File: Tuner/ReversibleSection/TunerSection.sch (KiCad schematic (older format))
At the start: 68 parts, among them J1 Conn_01x03, J10 Conn_01x02, J11 Conn_01x05, J12 Conn_01x01, J13 Conn_01x01, J14 Conn_01x01, J15 Conn_01x01, J2 Conn_01x03, J3 Conn_01x03, J4 Conn_01x03, J5 Conn_01x03, J6 Conn_01x03, J7 Conn_01x03, J8 Conn_01x02, J9 Conn_01x02, U1 MCP23008, U2 ULN2803A

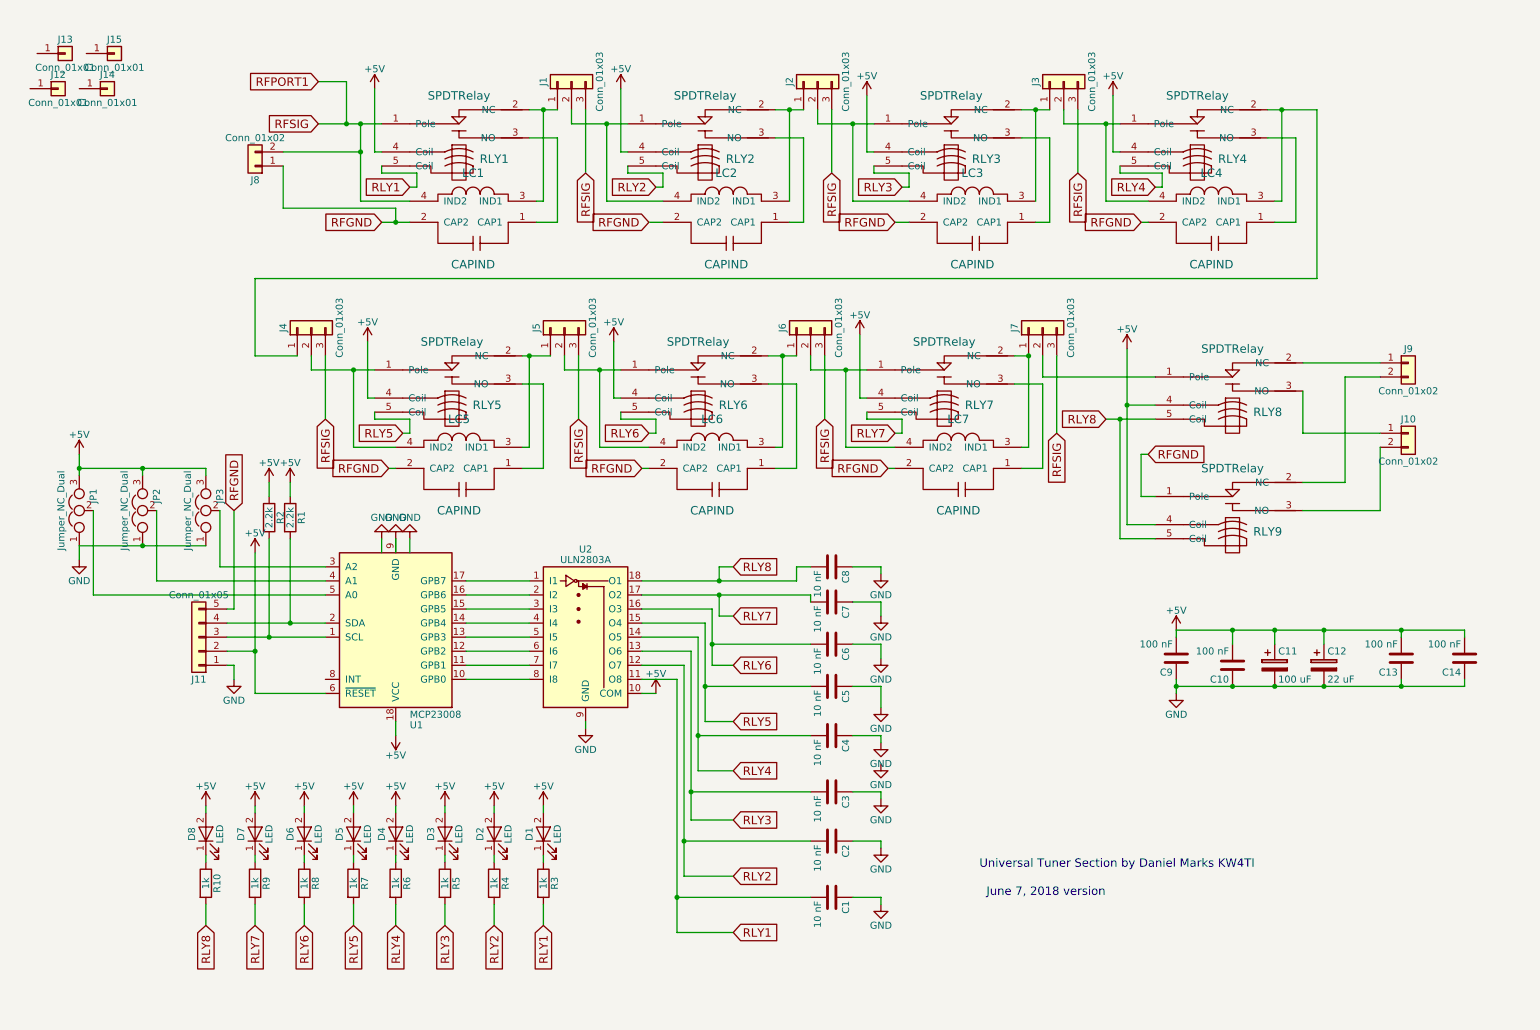
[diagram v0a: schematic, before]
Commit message: Added RF Shielding to ReversibleSection
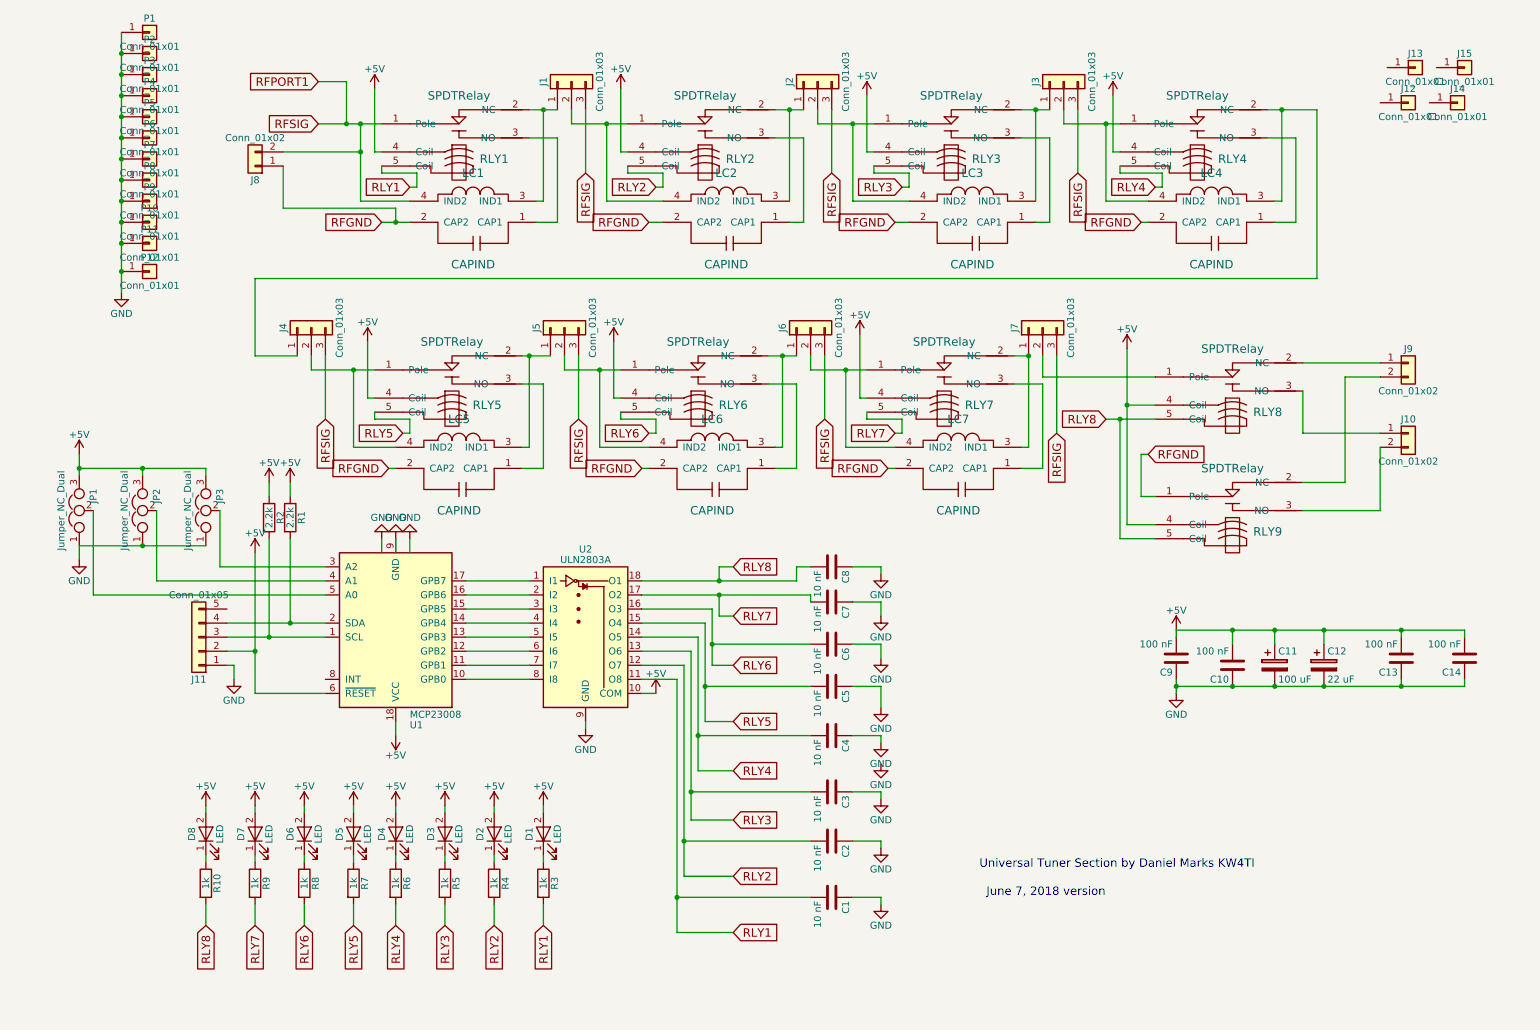
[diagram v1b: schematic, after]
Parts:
- added P1, P10, P11, P12, P2, P3, P4, P5, P6, P7, P8, P9: Conn_01x01, Pin_Headers:Pin_Header_Straight_1x01_Pitch2.54mm, symbol Conn_01x01
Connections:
- net GND: now also P1.1 (Pin_1), P10.1 (Pin_1), P11.1 (Pin_1), P12.1 (Pin_1), P2.1 (Pin_1), P3.1 (Pin_1), P4.1 (Pin_1), P5.1 (Pin_1), P6.1 (Pin_1), P7.1 (Pin_1), P8.1 (Pin_1), P9.1 (Pin_1)
- net RFGND: no longer J11.5 (Pin_5)
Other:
- moved on the sheet: J12, J13, J14, J15

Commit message: Modified RelayControl and Reversible Section to Isolate Digital from Analog sections using RF chokes
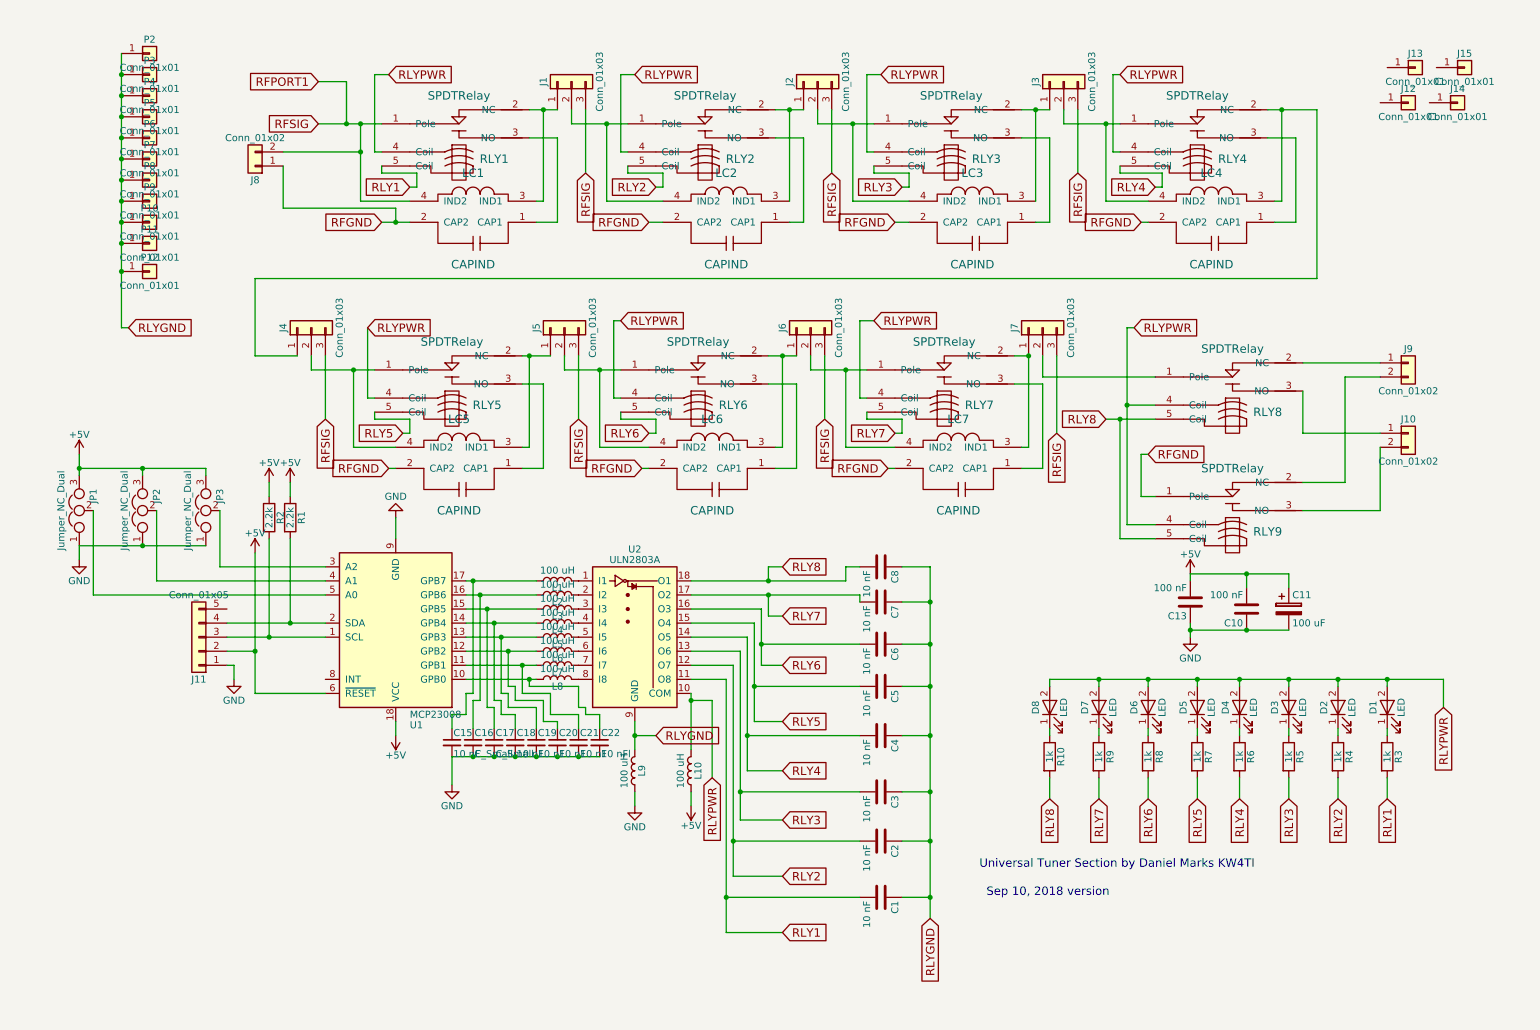
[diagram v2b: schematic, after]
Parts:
- removed C12: 22 uF, Capacitors_THT:CP_Radial_D5.0mm_P2.50mm, symbol CP
- removed C14, C9: 100 nF, Capacitors_THT:C_Disc_D5.0mm_W2.5mm_P2.50mm, symbol C
- removed P1: Conn_01x01, Pin_Headers:Pin_Header_Straight_1x01_Pitch2.54mm, symbol Conn_01x01
- added C15, C18, C19, C20, C21: 10 nF, Capacitors_THT:C_Disc_D5.0mm_W2.5mm_P2.50mm, symbol C_Small
- added C16, C17: C_Small, Capacitors_THT:C_Disc_D5.0mm_W2.5mm_P2.50mm, symbol C_Small
- added C22: 10 nFl, Capacitors_THT:C_Disc_D5.0mm_W2.5mm_P2.50mm, symbol C_Small
- added L1, L10, L2, L3, L4, L5, L6, L7, L8, L9: 100 uH, Inductors_THT:L_Axial_L5.3mm_D2.2mm_P7.62mm_Horizontal_Vishay_IM-1, symbol L
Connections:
- net +5V: now also L10.1; no longer D1.2 (A), D2.2 (A), D3.2 (A), D4.2 (A), D5.2 (A), D6.2 (A), D7.2 (A), D8.2 (A), RLY1.4 (Coil), RLY2.4 (Coil), RLY3.4 (Coil), RLY4.4 (Coil), RLY5.4 (Coil), RLY6.4 (Coil), RLY7.4 (Coil), RLY8.4 (Coil), RLY9.4 (Coil), U2.10 (COM)
- net GND: now also C15.2, C16.2, C17.2, C18.2, C19.2, C20.2, C21.2, C22.2, L9.1; no longer C1.1, C2.1, C3.1, C4.1, C5.1, C6.1, C7.1, C8.1, P10.1 (Pin_1), P11.1 (Pin_1), P12.1 (Pin_1), P2.1 (Pin_1), P3.1 (Pin_1), P4.1 (Pin_1), P5.1 (Pin_1), P6.1 (Pin_1), P7.1 (Pin_1), P8.1 (Pin_1), P9.1 (Pin_1), U2.9 (GND)
- net at U2.1 (I1): now also L1.2; no longer U1.17 (GPB7)
- net at U2.2 (I2): now also L2.2; no longer U1.16 (GPB6)
- net at U2.3 (I3): now also L3.2; no longer U1.15 (GPB5)
- net at U2.4 (I4): now also L4.2; no longer U1.14 (GPB4)
- net at U2.5 (I5): now also L5.2; no longer U1.13 (GPB3)
- net at U2.6 (I6): now also L6.2; no longer U1.12 (GPB2)
- net at U2.7 (I7): now also L7.2; no longer U1.11 (GPB1)
- net at U2.8 (I8): now also L8.2; no longer U1.10 (GPB0)
- new net: C22.1, L8.1, U1.10 (GPB0)
- new net: C21.1, L7.1, U1.11 (GPB1)
- new net: C20.1, L6.1, U1.12 (GPB2)
- new net: C19.1, L5.1, U1.13 (GPB3)
- new net: C18.1, L4.1, U1.14 (GPB4)
- new net: C17.1, L3.1, U1.15 (GPB5)
- new net: C16.1, L2.1, U1.16 (GPB6)
- new net: C15.1, L1.1, U1.17 (GPB7)
- new net RLYGND: C1.1, C2.1, C3.1, C4.1, C5.1, C6.1, C7.1, C8.1, L9.2, P10.1 (Pin_1), P11.1 (Pin_1), P12.1 (Pin_1), P2.1 (Pin_1), P3.1 (Pin_1), P4.1 (Pin_1), P5.1 (Pin_1), P6.1 (Pin_1), P7.1 (Pin_1), P8.1 (Pin_1), P9.1 (Pin_1), U2.9 (GND)
- new net RLYPWR: D1.2 (A), D2.2 (A), D3.2 (A), D4.2 (A), D5.2 (A), D6.2 (A), D7.2 (A), D8.2 (A), L10.2, RLY1.4 (Coil), RLY2.4 (Coil), RLY3.4 (Coil), RLY4.4 (Coil), RLY5.4 (Coil), RLY6.4 (Coil), RLY7.4 (Coil), RLY8.4 (Coil), RLY9.4 (Coil), U2.10 (COM)
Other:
- note added: "Sep 10, 2018 version"
- note removed: "June 7, 2018 version"
- moved on the sheet: C1, C10, C11, C13, C2, C3, C4, C5, C6, C7, C8, D1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

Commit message: Added extra filtering and shunt to RF ground
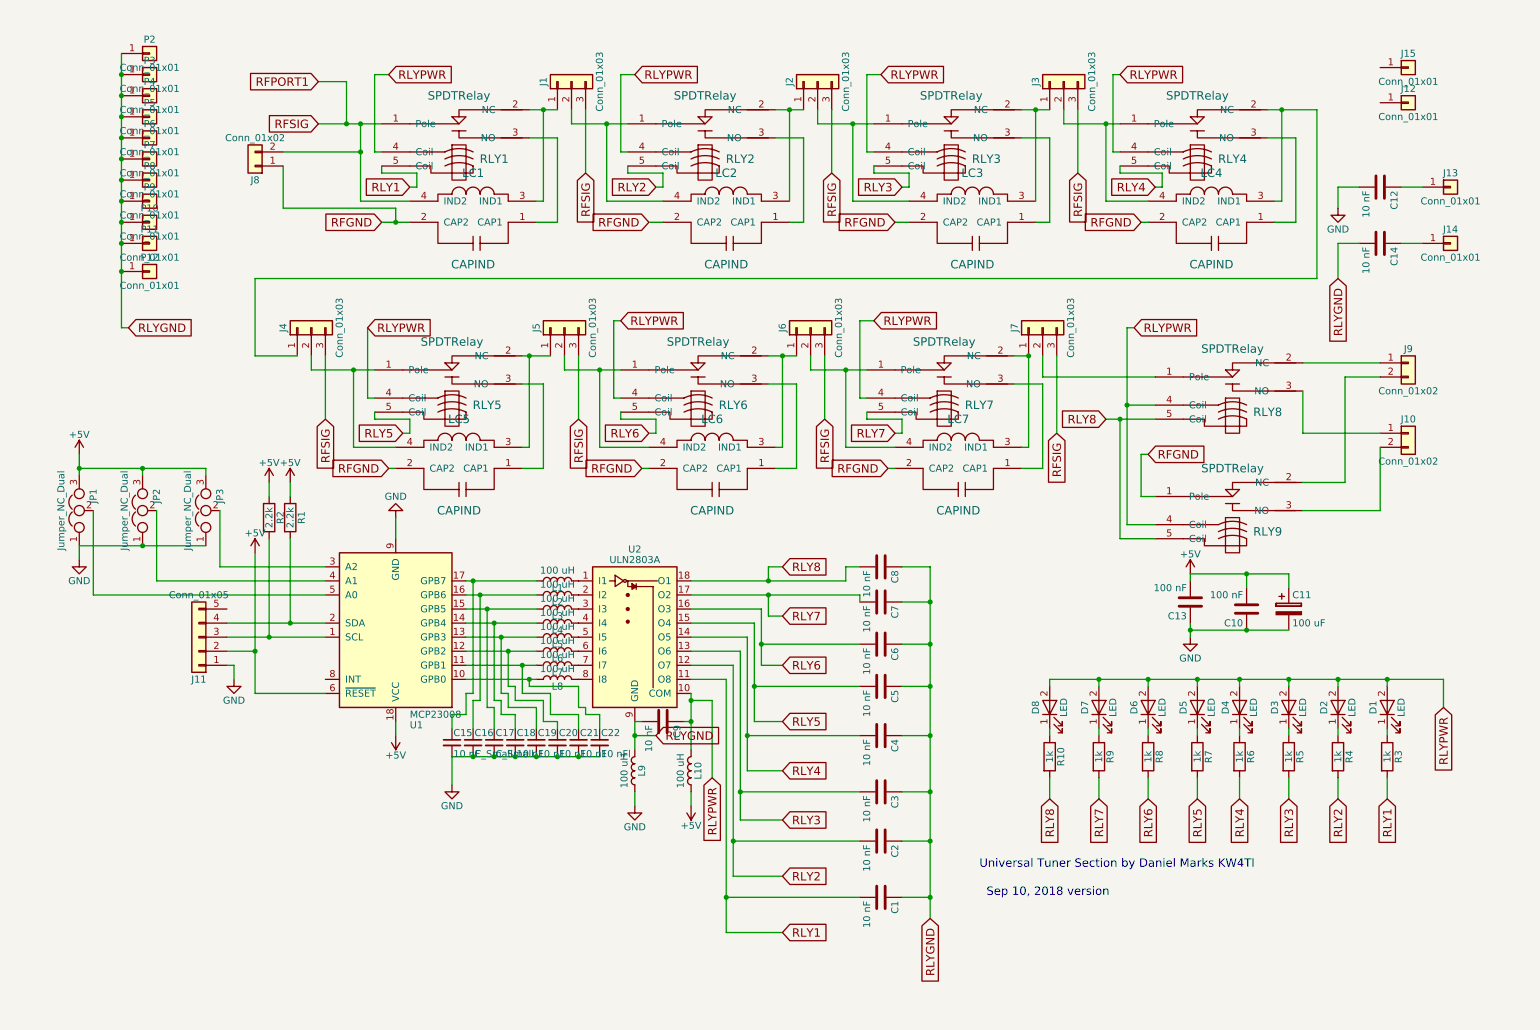
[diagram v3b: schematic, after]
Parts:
- added C12, C14, C9: 10 nF, Capacitors_THT:C_Disc_D5.0mm_W2.5mm_P2.50mm, symbol C
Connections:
- net GND: now also C12.2
- net RLYGND: now also C14.2, C9.2
- net RLYPWR: now also C9.1
- net at J13.1 (Pin_1): now also C12.1
- net at J14.1 (Pin_1): now also C14.1
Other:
- moved on the sheet: J13, J14, J15
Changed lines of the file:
@@
 L Conn_01x01 J13
 U 1 1 5B19804D
-P 10400 1000
-F 0 "J13" H 10400 1100 50  0000 C CNN
-F 1 "Conn_01x01" H 10400 900 50  0000 C CNN
-F 2 "Connectors:1pin" H 10400 1000 50  0001 C CNN
-F 3 "" H 10400 1000 50  0001 C CNN
-	1    10400 1000
+P 10650 1850
+F 0 "J13" H 10650 1950 50  0000 C CNN
+F 1 "Conn_01x01" H 10650 1750 50  0000 C CNN
+F 2 "Connectors:1pin" H 10650 1850 50  0001 C CNN
+F 3 "" H 10650 1850 50  0001 C CNN
+	1    10650 1850
 	1    0    0    -1
 $EndComp
@@
 L Conn_01x01 J15
 U 1 1 5B19812D
-P 10750 1000
-F 0 "J15" H 10750 1100 50  0000 C CNN
-F 1 "Conn_01x01" H 10750 900 50  0000 C CNN
-F 2 "Connectors:1pin" H 10750 1000 50  0001 C CNN
-F 3 "" H 10750 1000 50  0001 C CNN
-	1    10750 1000
+P 10350 1000
+F 0 "J15" H 10350 1100 50  0000 C CNN
+F 1 "Conn_01x01" H 10350 900 50  0000 C CNN
+F 2 "Connectors:1pin" H 10350 1000 50  0001 C CNN
+F 3 "" H 10350 1000 50  0001 C CNN
+	1    10350 1000
 	1    0    0    -1
 $EndComp
@@
 L Conn_01x01 J14
 U 1 1 5B198288
-P 10700 1250
-F 0 "J14" H 10700 1350 50  0000 C CNN
-F 1 "Conn_01x01" H 10700 1150 50  0000 C CNN
-F 2 "Connectors:1pin" H 10700 1250 50  0001 C CNN
-F 3 "" H 10700 1250 50  0001 C CNN
-	1    10700 1250
+P 10650 2250
+F 0 "J14" H 10650 2350 50  0000 C CNN
+F 1 "Conn_01x01" H 10650 2150 50  0000 C CNN
+F 2 "Connectors:1pin" H 10650 2250 50  0001 C CNN
+F 3 "" H 10650 2250 50  0001 C CNN
+	1    10650 2250
 	1    0    0    -1
 $EndComp
@@
 Wire Wire Line
 	2950 3350 2950 2850
+$Comp
+L C C9
+U 1 1 5B972534
+P 5050 5650
+F 0 "C9" H 5075 5750 50  0000 L CNN
+F 1 "10 nF" H 5075 5550 50  0000 L CNN
+F 2 "Capacitors_THT:C_Disc_D5.0mm_W2.5mm_P2.50mm" H 5088 5500 50  0001 C CNN
+F 3 "" H 5050 5650 50  0001 C CNN
+	1    5050 5650
+	0    1    1    0
+$EndComp
+Wire Wire Line
+	4900 5650 4850 5650
+Wire Wire Line
+	5200 5650 5250 5650
+Connection ~ 5250 5650
+$Comp
+L C C12
+U 1 1 5B9823B9
+P 10150 1850
+F 0 "C12" H 10175 1950 50  0000 L CNN
+F 1 "10 nF" H 10175 1750 50  0000 L CNN
+F 2 "Capacitors_THT:C_Disc_D5.0mm_W2.5mm_P2.50mm" H 10188 1700 50  0001 C CNN
+F 3 "" H 10150 1850 50  0001 C CNN
+	1    10150 1850
+	0    1    1    0
+$EndComp
+$Comp
+L GND #PWR014
+U 1 1 5B982525
+P 9850 2000
+F 0 "#PWR014" H 9850 1750 50  0001 C CNN
+F 1 "GND" H 9850 1850 50  0000 C CNN
+F 2 "" H 9850 2000 50  0001 C CNN
+F 3 "" H 9850 2000 50  0001 C CNN
+	1    9850 2000
+	1    0    0    -1
+$EndComp
+Wire Wire Line
+	9850 2000 9850 1850
+Wire Wire Line
+	9850 1850 10000 1850
+Wire Wire Line
+	10300 1850 10450 1850
+Text GLabel 9850 2500 3    60   Input ~ 0
+RLYGND
+$Comp
+L C C14
+U 1 1 5B9838B1
+P 10150 2250
+F 0 "C14" H 10175 2350 50  0000 L CNN
+F 1 "10 nF" H 10175 2150 50  0000 L CNN
+F 2 "Capacitors_THT:C_Disc_D5.0mm_W2.5mm_P2.50mm" H 10188 2100 50  0001 C CNN
+F 3 "" H 10150 2250 50  0001 C CNN
+	1    10150 2250
+	0    1    1    0
+$EndComp
+Wire Wire Line
+	10300 2250 10450 2250
+Wire Wire Line
+	9850 2500 9850 2250
+Wire Wire Line
+	9850 2250 10000 2250
 $EndSCHEMATC
